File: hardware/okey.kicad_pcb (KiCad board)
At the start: 2 copper layers, 243.8 x 352.4 mm, 116 parts, among them IC1 4094N, IC2 4094N, P1 ROW_JMP, P10 CONN_02X06, P11 CONN_02X06, P12 CONN_02X06, P13 CONN_02X06, P14 CONN_02X06, P15 CONN_02X06, P16 CONN_02X08, P17 CONN_01X01, P18 CONN_02X08, P19 CONN_01X01, P2 CONN_02X13, P20 CONN_01X01, P21 CONN_01X01, P22 CONN_02X08, P23 CONN_02X08, P24 CONN_02X06, P25 CONN_02X06, P26 CONN_02X06, P27 CONN_02X06, P28 CONN_02X06, P29 CONN_02X06, P3 CONN_02X03, P30 CONN_02X08, P31 CONN_02X03, P4 CONN_02X08, P5 CONN_02X03, P6 CONN_02X10, P7 CONN_02X03, P8 CONN_01X01, P9 CONN_02X08, Q1 Q_NPN_BCE, Q2 Q_NPN_BCE, Q3 Q_NPN_BCE, SW1 MX_D, SW10 MX_D, SW11 MX_D, SW12 MX_D, SW13 MX_D, SW14 MX_D, SW15 MX_D, SW16 MX_D, SW17 MX_D, SW18 MX_D, SW19 SW_PUSH, SW2 MX_D, SW20 SW_PUSH, SW21 SW_PUSH, SW22 SW_PUSH, SW23 SW_PUSH, SW24 SW_PUSH, SW25 SW_PUSH, SW26 SW_PUSH, SW27 SW_PUSH, SW28 SW_PUSH, SW29 SW_PUSH, SW3 MX_D, SW30 SW_PUSH, SW31 SW_PUSH, SW32 SW_PUSH, SW33 SW_PUSH, SW34 SW_PUSH, SW35 MX_D, SW36 MX_D, SW37 MX_D, SW38 MX_D, SW39 MX_D, SW4 MX_D, SW5 MX_D, SW6 MX_D, SW7 MX_D, SW8 MX_D, SW9 MX_D, U1 4053, U2 4024, U3 TEENSY2.0

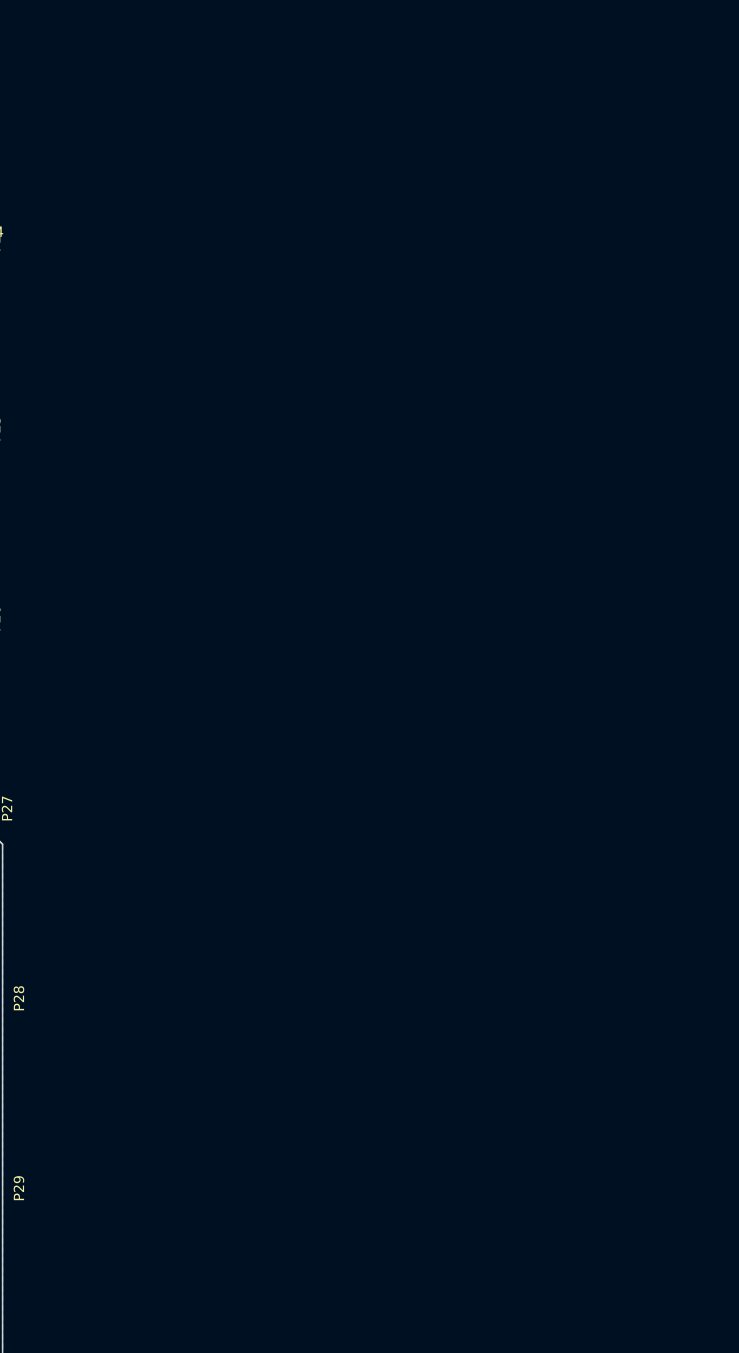
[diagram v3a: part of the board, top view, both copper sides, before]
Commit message: hardware: reworked key columns PCB
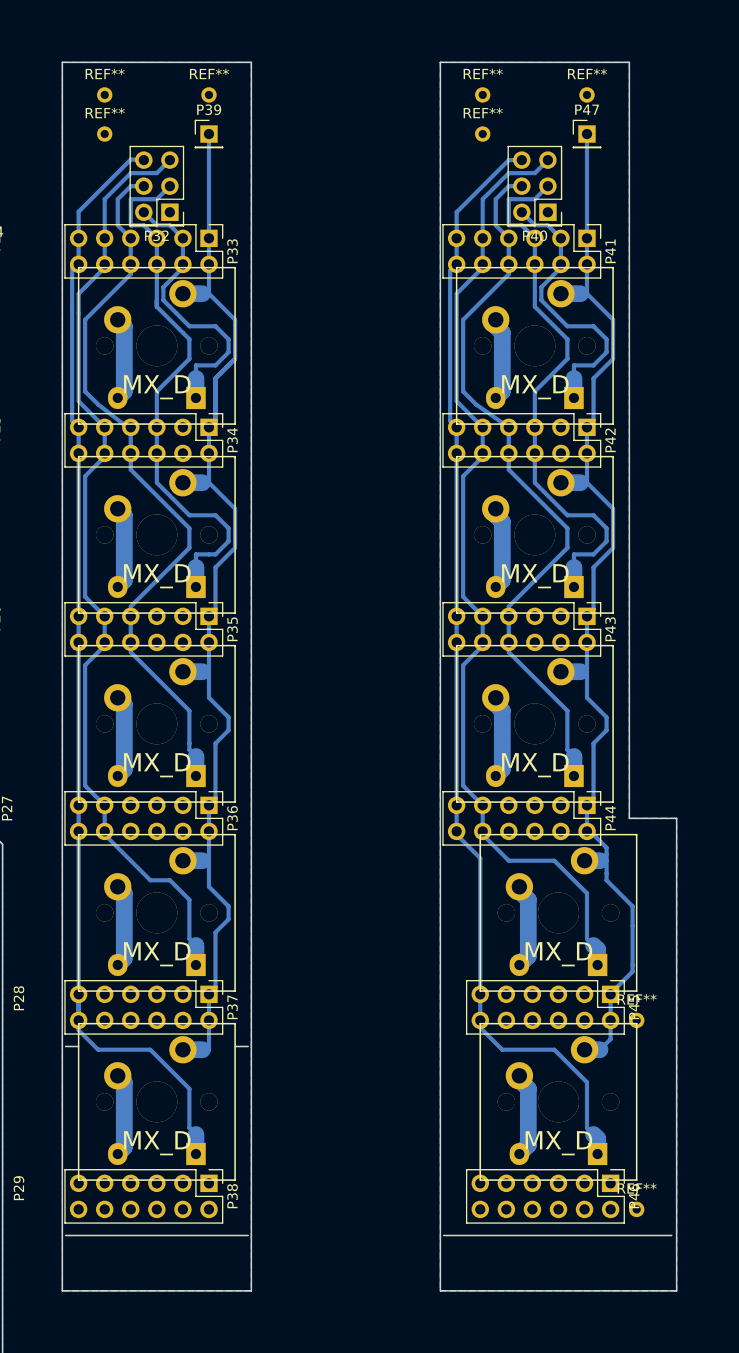
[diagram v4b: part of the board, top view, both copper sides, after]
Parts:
- added P32: CONN_02X03, Pin_Headers:Pin_Header_Straight_2x03_Pitch2.54mm, F.Cu at (140.0, 135.0)
- added P33: CONN_02X06, Pin_Headers:Pin_Header_Straight_2x06_Pitch2.54mm, F.Cu at (137.5, 138.8)
- added P34: CONN_02X06, Pin_Headers:Pin_Header_Straight_2x06_Pitch2.54mm, F.Cu at (137.5, 157.2)
- added P35: CONN_02X06, Pin_Headers:Pin_Header_Straight_2x06_Pitch2.54mm, F.Cu at (137.5, 175.6)
- added P36: CONN_02X06, Pin_Headers:Pin_Header_Straight_2x06_Pitch2.54mm, F.Cu at (137.5, 194.0)
- added P37: CONN_02X06, Pin_Headers:Pin_Header_Straight_2x06_Pitch2.54mm, F.Cu at (137.5, 212.5)
- added P38: CONN_02X06, Pin_Headers:Pin_Header_Straight_2x06_Pitch2.54mm, F.Cu at (137.5, 230.9)
- added P39: CONN_01X01, Pin_Headers:Pin_Header_Straight_1x01_Pitch2.54mm, F.Cu at (143.8, 127.4)
- added P40: CONN_02X03, Pin_Headers:Pin_Header_Straight_2x03_Pitch2.54mm, F.Cu at (176.8, 135.0)
- added P41: CONN_02X06, Pin_Headers:Pin_Header_Straight_2x06_Pitch2.54mm, F.Cu at (174.3, 138.8)
- added P42: CONN_02X06, Pin_Headers:Pin_Header_Straight_2x06_Pitch2.54mm, F.Cu at (174.3, 157.2)
- added P43: CONN_02X06, Pin_Headers:Pin_Header_Straight_2x06_Pitch2.54mm, F.Cu at (174.3, 175.6)
- added P44: CONN_02X06, Pin_Headers:Pin_Header_Straight_2x06_Pitch2.54mm, F.Cu at (174.3, 194.0)
- added P45: CONN_02X06, Pin_Headers:Pin_Header_Straight_2x06_Pitch2.54mm, F.Cu at (176.6, 212.5)
- added P46: CONN_02X06, Pin_Headers:Pin_Header_Straight_2x06_Pitch2.54mm, F.Cu at (176.6, 230.9)
- added P47: CONN_01X01, Pin_Headers:Pin_Header_Straight_1x01_Pitch2.54mm, F.Cu at (180.7, 127.4)
- added REF**: Measurement_Point_Round-TH_Small, Measurement_Points:Measurement_Point_Round-TH_Small, F.Cu at (133.7, 127.4)
- added REF**: Measurement_Point_Round-TH_Small, Measurement_Points:Measurement_Point_Round-TH_Small, F.Cu at (133.7, 123.6)
- added REF**: Measurement_Point_Round-TH_Small, Measurement_Points:Measurement_Point_Round-TH_Small, F.Cu at (143.8, 123.6)
- added REF**: Measurement_Point_Round-TH_Small, Measurement_Points:Measurement_Point_Round-TH_Small, F.Cu at (170.5, 127.4)
- added REF**: Measurement_Point_Round-TH_Small, Measurement_Points:Measurement_Point_Round-TH_Small, F.Cu at (170.5, 123.6)
- added REF**: Measurement_Point_Round-TH_Small, Measurement_Points:Measurement_Point_Round-TH_Small, F.Cu at (180.7, 123.6)
- added REF**: Measurement_Point_Round-TH_Small, Measurement_Points:Measurement_Point_Round-TH_Small, F.Cu at (185.5, 213.7)
- added REF**: Measurement_Point_Round-TH_Small, Measurement_Points:Measurement_Point_Round-TH_Small, F.Cu at (185.5, 232.1)
- added SW40: MX_D, cherry:SW_PCB_4PIN, F.Cu at (138.8, 148.0)
- added SW41: MX_D, cherry:SW_PCB_4PIN, F.Cu at (138.8, 166.4)
- added SW42: MX_D, cherry:SW_PCB_4PIN, F.Cu at (138.8, 184.8)
- added SW43: MX_D, cherry:SW_PCB_4PIN, F.Cu at (138.8, 203.3)
- added SW44: MX_D, cherry:SW_PCB_4PIN, F.Cu at (138.8, 221.7)
- added SW45: MX_D, cherry:SW_PCB_4PIN, F.Cu at (175.6, 148.0)
- added SW46: MX_D, cherry:SW_PCB_4PIN, F.Cu at (175.6, 166.4)
- added SW47: MX_D, cherry:SW_PCB_4PIN, F.Cu at (175.6, 184.8)
- added SW48: MX_D, cherry:SW_PCB_4PIN, F.Cu at (177.9, 203.3)
- added SW49: MX_D, cherry:SW_PCB_4PIN, F.Cu at (177.9, 221.7)
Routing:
- net Net-(P33-Pad1): track 0.00 -> 117.1 mm
- net Net-(P40-Pad6): track 0.00 -> 111.2 mm
- net Net-(P32-Pad6): track 0.00 -> 111.2 mm
- net Net-(P41-Pad1): track 0.00 -> 109.6 mm
- net Net-(P40-Pad5): track 0.00 -> 95.6 mm
- net Net-(P32-Pad5): track 0.00 -> 93.0 mm
- net Net-(P32-Pad4): track 0.00 -> 71.2 mm
- net Net-(P40-Pad4): track 0.00 -> 71.2 mm
- net Net-(P32-Pad3): track 0.00 -> 55.0 mm
- net Net-(P40-Pad3): track 0.00 -> 53.4 mm
- net Net-(P40-Pad2): track 0.00 -> 28.4 mm
- net Net-(P32-Pad2): track 0.00 -> 27.8 mm
- net Net-(SW40-Pad2): track 0.00 -> 15.4 mm
- net Net-(SW49-Pad2): track 0.00 -> 8.34 mm
- net Net-(SW48-Pad2): track 0.00 -> 8.34 mm
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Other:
- outline, holes or cut-outs redrawn

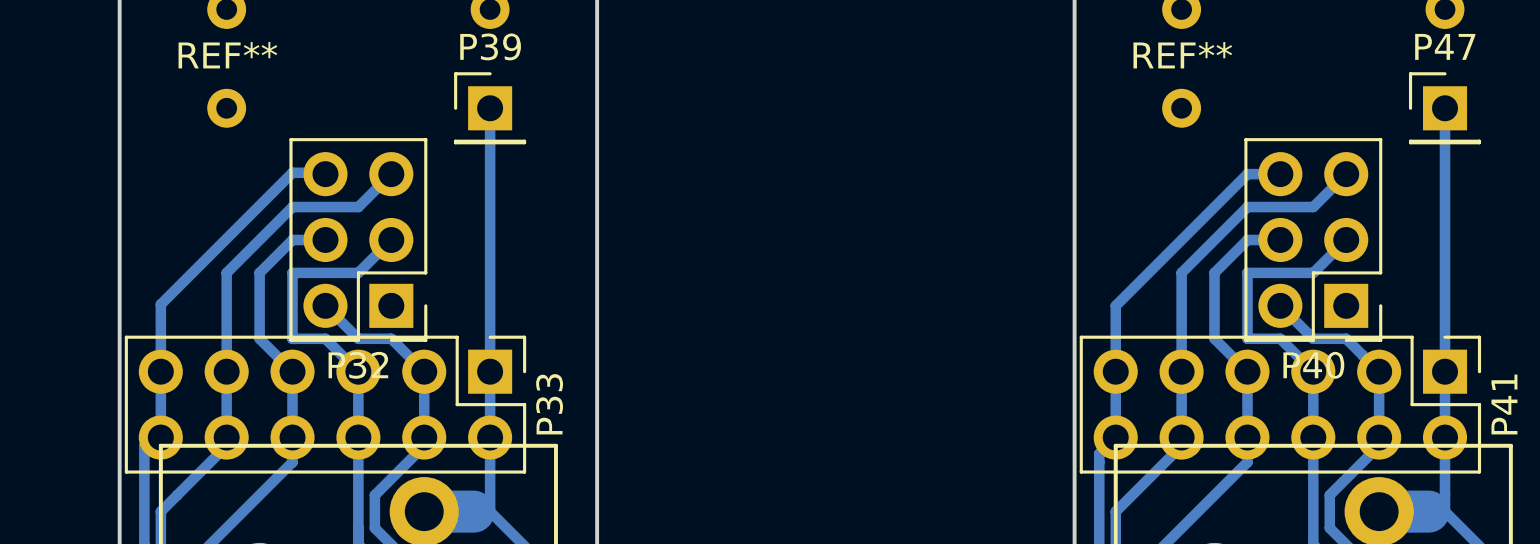
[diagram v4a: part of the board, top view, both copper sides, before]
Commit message: squash! hardware: reworked key columns PCB
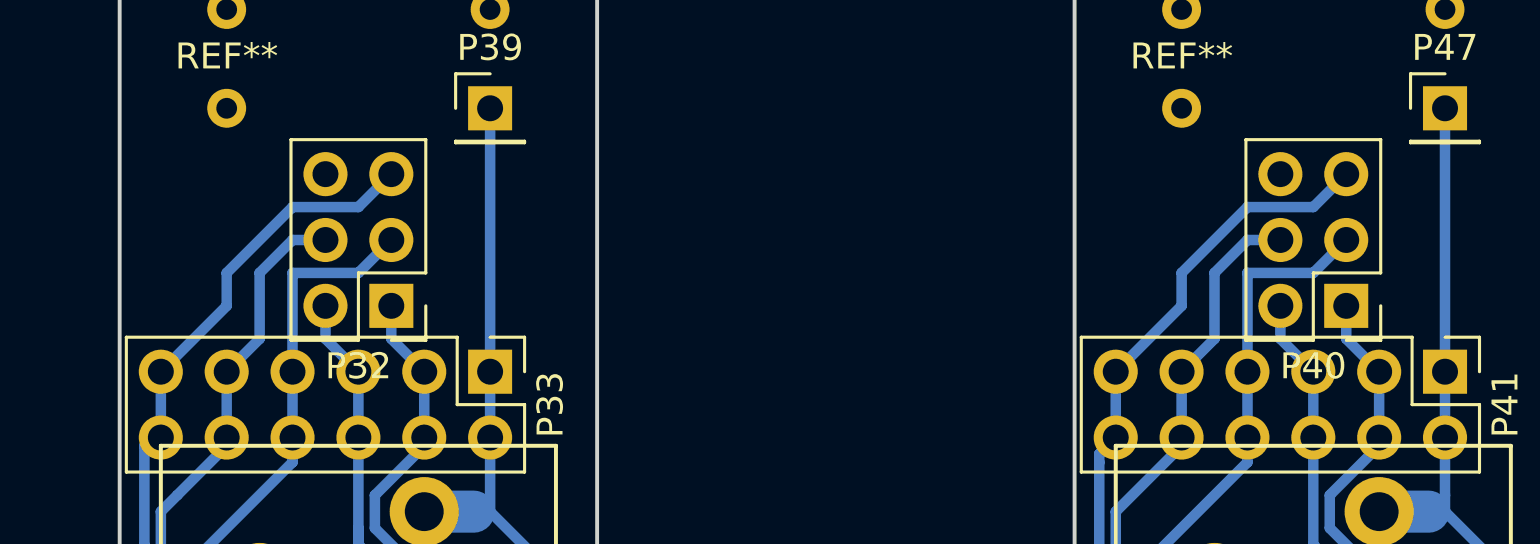
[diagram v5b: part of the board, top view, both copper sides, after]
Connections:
- P32 pad 1: GND -> Net-(P32-Pad1)
- P32 pad 6: Net-(P32-Pad6) -> GND
- P33 pad 10: Net-(P32-Pad5) -> Net-(P32-Pad4)
- P33 pad 11: Net-(P32-Pad6) -> Net-(P32-Pad5)
- P33 pad 12: Net-(P32-Pad6) -> Net-(P32-Pad5)
- P33 pad 3: Net-(P32-Pad2) -> Net-(P32-Pad1)
- P33 pad 4: Net-(P32-Pad2) -> Net-(P32-Pad1)
- P33 pad 5: Net-(P32-Pad3) -> Net-(P32-Pad2)
- P33 pad 6: Net-(P32-Pad3) -> Net-(P32-Pad2)
- P33 pad 7: Net-(P32-Pad4) -> Net-(P32-Pad3)
- P33 pad 8: Net-(P32-Pad4) -> Net-(P32-Pad3)
- P33 pad 9: Net-(P32-Pad5) -> Net-(P32-Pad4)
- P34 pad 10: Net-(P32-Pad5) -> Net-(P32-Pad4)
- P34 pad 11: Net-(P32-Pad6) -> Net-(P32-Pad5)
- P34 pad 12: Net-(P32-Pad6) -> Net-(P32-Pad5)
- P34 pad 5: Net-(P32-Pad3) -> Net-(P32-Pad2)
- P34 pad 6: Net-(P32-Pad3) -> Net-(P32-Pad2)
- P34 pad 7: Net-(P32-Pad4) -> Net-(P32-Pad3)
- P34 pad 8: Net-(P32-Pad4) -> Net-(P32-Pad3)
- P34 pad 9: Net-(P32-Pad5) -> Net-(P32-Pad4)
- P35 pad 10: Net-(P32-Pad5) -> Net-(P32-Pad4)
- P35 pad 11: Net-(P32-Pad6) -> Net-(P32-Pad5)
- P35 pad 12: Net-(P32-Pad6) -> Net-(P32-Pad5)
- P35 pad 7: Net-(P32-Pad4) -> Net-(P32-Pad3)
- P35 pad 8: Net-(P32-Pad4) -> Net-(P32-Pad3)
- P35 pad 9: Net-(P32-Pad5) -> Net-(P32-Pad4)
- P36 pad 10: Net-(P32-Pad5) -> Net-(P32-Pad4)
- P36 pad 11: Net-(P32-Pad6) -> Net-(P32-Pad5)
- P36 pad 12: Net-(P32-Pad6) -> Net-(P32-Pad5)
- P36 pad 9: Net-(P32-Pad5) -> Net-(P32-Pad4)
- P37 pad 11: Net-(P32-Pad6) -> Net-(P32-Pad5)
- P37 pad 12: Net-(P32-Pad6) -> Net-(P32-Pad5)
- P40 pad 1: GND -> Net-(P40-Pad1)
- P40 pad 6: Net-(P40-Pad6) -> GND
- P41 pad 10: Net-(P40-Pad5) -> Net-(P40-Pad4)
- P41 pad 11: Net-(P40-Pad6) -> Net-(P40-Pad5)
- P41 pad 12: Net-(P40-Pad6) -> Net-(P40-Pad5)
- P41 pad 3: Net-(P40-Pad2) -> Net-(P40-Pad1)
- P41 pad 4: Net-(P40-Pad2) -> Net-(P40-Pad1)
- P41 pad 5: Net-(P40-Pad3) -> Net-(P40-Pad2)
- P41 pad 6: Net-(P40-Pad3) -> Net-(P40-Pad2)
- P41 pad 7: Net-(P40-Pad4) -> Net-(P40-Pad3)
- P41 pad 8: Net-(P40-Pad4) -> Net-(P40-Pad3)
- P41 pad 9: Net-(P40-Pad5) -> Net-(P40-Pad4)
- P42 pad 10: Net-(P40-Pad5) -> Net-(P40-Pad4)
- P42 pad 11: Net-(P40-Pad6) -> Net-(P40-Pad5)
- P42 pad 12: Net-(P40-Pad6) -> Net-(P40-Pad5)
- P42 pad 5: Net-(P40-Pad3) -> Net-(P40-Pad2)
- P42 pad 6: Net-(P40-Pad3) -> Net-(P40-Pad2)
- P42 pad 7: Net-(P40-Pad4) -> Net-(P40-Pad3)
- P42 pad 8: Net-(P40-Pad4) -> Net-(P40-Pad3)
- P42 pad 9: Net-(P40-Pad5) -> Net-(P40-Pad4)
- P43 pad 10: Net-(P40-Pad5) -> Net-(P40-Pad4)
- P43 pad 11: Net-(P40-Pad6) -> Net-(P40-Pad5)
- P43 pad 12: Net-(P40-Pad6) -> Net-(P40-Pad5)
- P43 pad 7: Net-(P40-Pad4) -> Net-(P40-Pad3)
- P43 pad 8: Net-(P40-Pad4) -> Net-(P40-Pad3)
- P43 pad 9: Net-(P40-Pad5) -> Net-(P40-Pad4)
- P44 pad 10: Net-(P40-Pad5) -> Net-(P40-Pad4)
- P44 pad 11: Net-(P40-Pad6) -> Net-(P40-Pad5)
- P44 pad 12: Net-(P40-Pad6) -> Net-(P40-Pad5)
- P44 pad 9: Net-(P40-Pad5) -> Net-(P40-Pad4)
- P45 pad 11: Net-(P40-Pad6) -> Net-(P40-Pad5)
- P45 pad 12: Net-(P40-Pad6) -> Net-(P40-Pad5)
- SW40 pad 4: Net-(P32-Pad2) -> Net-(P32-Pad1)
- SW41 pad 4: Net-(P32-Pad3) -> Net-(P32-Pad2)
- SW42 pad 4: Net-(P32-Pad4) -> Net-(P32-Pad3)
- SW43 pad 4: Net-(P32-Pad5) -> Net-(P32-Pad4)
- SW44 pad 4: Net-(P32-Pad6) -> Net-(P32-Pad5)
- SW45 pad 4: Net-(P40-Pad2) -> Net-(P40-Pad1)
- SW46 pad 4: Net-(P40-Pad3) -> Net-(P40-Pad2)
- SW47 pad 4: Net-(P40-Pad4) -> Net-(P40-Pad3)
- SW48 pad 4: Net-(P40-Pad5) -> Net-(P40-Pad4)
- SW49 pad 4: Net-(P40-Pad6) -> Net-(P40-Pad5)
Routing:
- net Net-(P40-Pad6): track 111.2 -> 0.00 mm
- net Net-(P32-Pad6): track 111.2 -> 0.00 mm
- net Net-(P40-Pad1): track 0.00 -> 26.6 mm
- net Net-(P32-Pad1): track 0.00 -> 26.0 mm
- net Net-(P40-Pad4): track 71.2 -> 91.3 mm
- net Net-(P32-Pad5): track 93.0 -> 113.0 mm
- net Net-(P32-Pad2): track 27.8 -> 47.9 mm
- net Net-(P40-Pad3): track 53.4 -> 71.9 mm
- net Net-(P40-Pad2): track 28.4 -> 46.5 mm
- net Net-(P40-Pad5): track 95.6 -> 113.0 mm
- net Net-(P32-Pad4): track 71.2 -> 88.6 mm
- net Net-(P32-Pad3): track 55.0 -> 72.0 mm

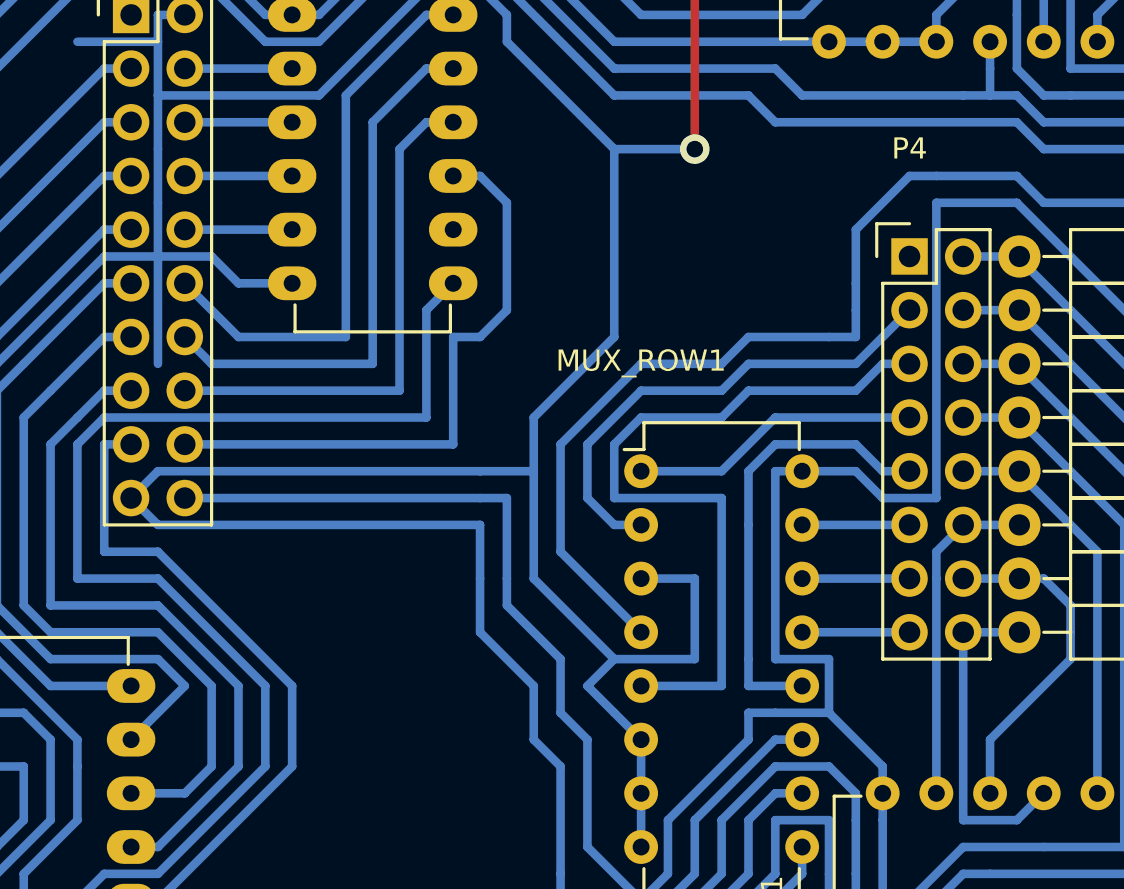
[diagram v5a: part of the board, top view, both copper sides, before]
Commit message: tidy up KSW_BUS connector
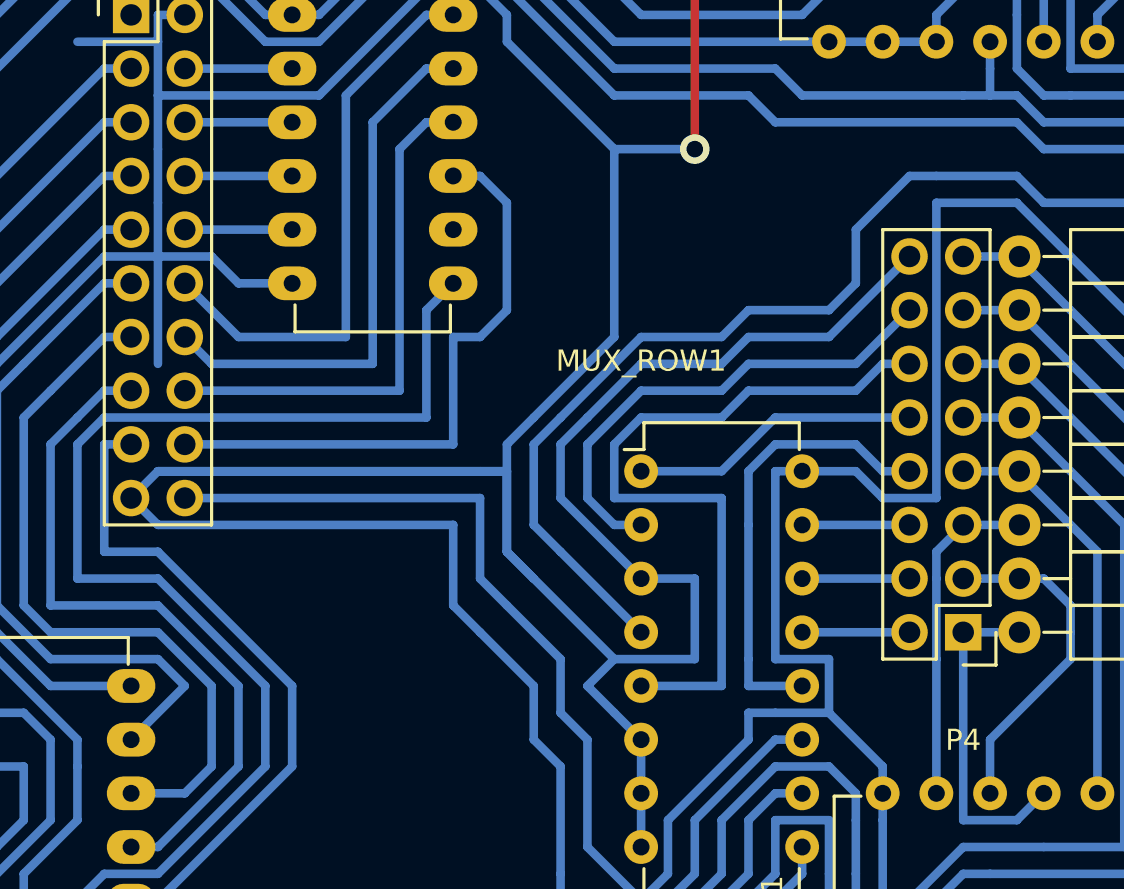
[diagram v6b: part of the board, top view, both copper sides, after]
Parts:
- moved P4 18.0 mm to (73.7, 61.0), turned to 180 degrees
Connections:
- P4 pad 1: (no net) -> Net-(D1-Pad2)
- P4 pad 10: Net-(D4-Pad2) -> Net-(MUX_ROW1-Pad1)
- P4 pad 11: Net-(MUX_ROW1-Pad15) -> Net-(D6-Pad2)
- P4 pad 12: Net-(D3-Pad2) -> Net-(MUX_ROW1-Pad5)
- P4 pad 13: Net-(MUX_ROW1-Pad14) -> Net-(D7-Pad2)
- P4 pad 14: Net-(D2-Pad2) -> Net-(MUX_ROW1-Pad2)
- P4 pad 15: Net-(MUX_ROW1-Pad13) -> Net-(D8-Pad2)
- P4 pad 16: Net-(D1-Pad2) -> GND
- P4 pad 2: Net-(D8-Pad2) -> Net-(MUX_ROW1-Pad13)
- P4 pad 3: Net-(MUX_ROW1-Pad2) -> Net-(D2-Pad2)
- P4 pad 4: Net-(D7-Pad2) -> Net-(MUX_ROW1-Pad14)
- P4 pad 5: Net-(MUX_ROW1-Pad5) -> Net-(D3-Pad2)
- P4 pad 6: Net-(D6-Pad2) -> Net-(MUX_ROW1-Pad15)
- P4 pad 7: Net-(MUX_ROW1-Pad1) -> Net-(D4-Pad2)
- P4 pad 8: Net-(D5-Pad2) -> Net-(MUX_ROW1-Pad12)
- P4 pad 9: Net-(MUX_ROW1-Pad12) -> Net-(D5-Pad2)
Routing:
- net GND: track 346.2 -> 395.5 mm
- net VDD: track 423.8 -> 423.1 mm
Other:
- board text added: "<- Grid Origin: 137.48 mm 138.8025 mm"
- board text added: "Absolute Origin"
